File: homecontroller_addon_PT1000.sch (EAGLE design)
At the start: 44 parts, among them U1 OPA2188AIDGKR, U2 OPA2188AIDGKR, U3 REF3025AIDBZTG4, U4 ADS1015IDGST, X1 S2L3.50/10/90G

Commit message: update routing
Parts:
- added C10: 1000pF, supply2:C1206C102KDRACTU
- added R26: 0 Ohms, Vishay_By_element14_Batch_1:CRCW12060000Z0EA
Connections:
- net N$5 renamed -IN_0
- removed net +IN_1: R12.2, U1.+IN_B
- removed net +IN_2: R19.2, U2.+IN_A
- removed net +IN_3: R25.2, U2.+IN_B
- removed net N$1: R6.2, U1.+IN_A
- new net PE: C10.C1, RV1.1, RV2.1, RV3.1, RV4.1
- new net SGND: C1.C1, C4.C1, C8.C1, C9.C1, R26.2
- net AGND: now also C10.C2, R26.1, X1.2, X1.4, X1.6, X1.8; no longer C1.C1, C4.C1, C8.C1, C9.C1, RV1.1, RV2.1, RV3.1, RV4.1, X1.1, X1.3, X1.5, X1.7
- net PT1000_0: now also R6.2, U1.+IN_A, X1.1; no longer X1.2
- net PT1000_1: now also R12.2, U1.+IN_B, X1.3; no longer X1.4
- net PT1000_2: now also R19.2, U2.+IN_A, X1.5; no longer X1.6
- net PT1000_3: now also R25.2, U2.+IN_B, X1.7; no longer X1.8
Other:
- moved on the sheet: R11, R18, R24, R5

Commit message: production status
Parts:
- U4: device strasys_standard:ADS1015IDGST -> ADS1015:ADS1015IDGST
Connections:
- net +3.3V: now also X2.10; no longer X2.1
- net AGND: now also X2.1; no longer X2.10
- net AIN2: now also U4.NC_2; no longer U4.AIN2
- net AIN3: now also U4.NC; no longer U4.AIN3
- net I2C1_SCL: now also X2.3; no longer X2.8
- net I2C1_SDA: now also X2.4; no longer X2.7
- net P9_14: now also X2.7; no longer X2.4
- net P9_15: now also X2.8; no longer X2.3
- net P9_16: now also X2.9; no longer X2.2
- net UART2_RXD: now also X2.6; no longer X2.5
- net UART2_TXD: now also X2.5; no longer X2.6
- net VDD5V_F: now also X2.2; no longer X2.9
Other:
- moved on the sheet: X2

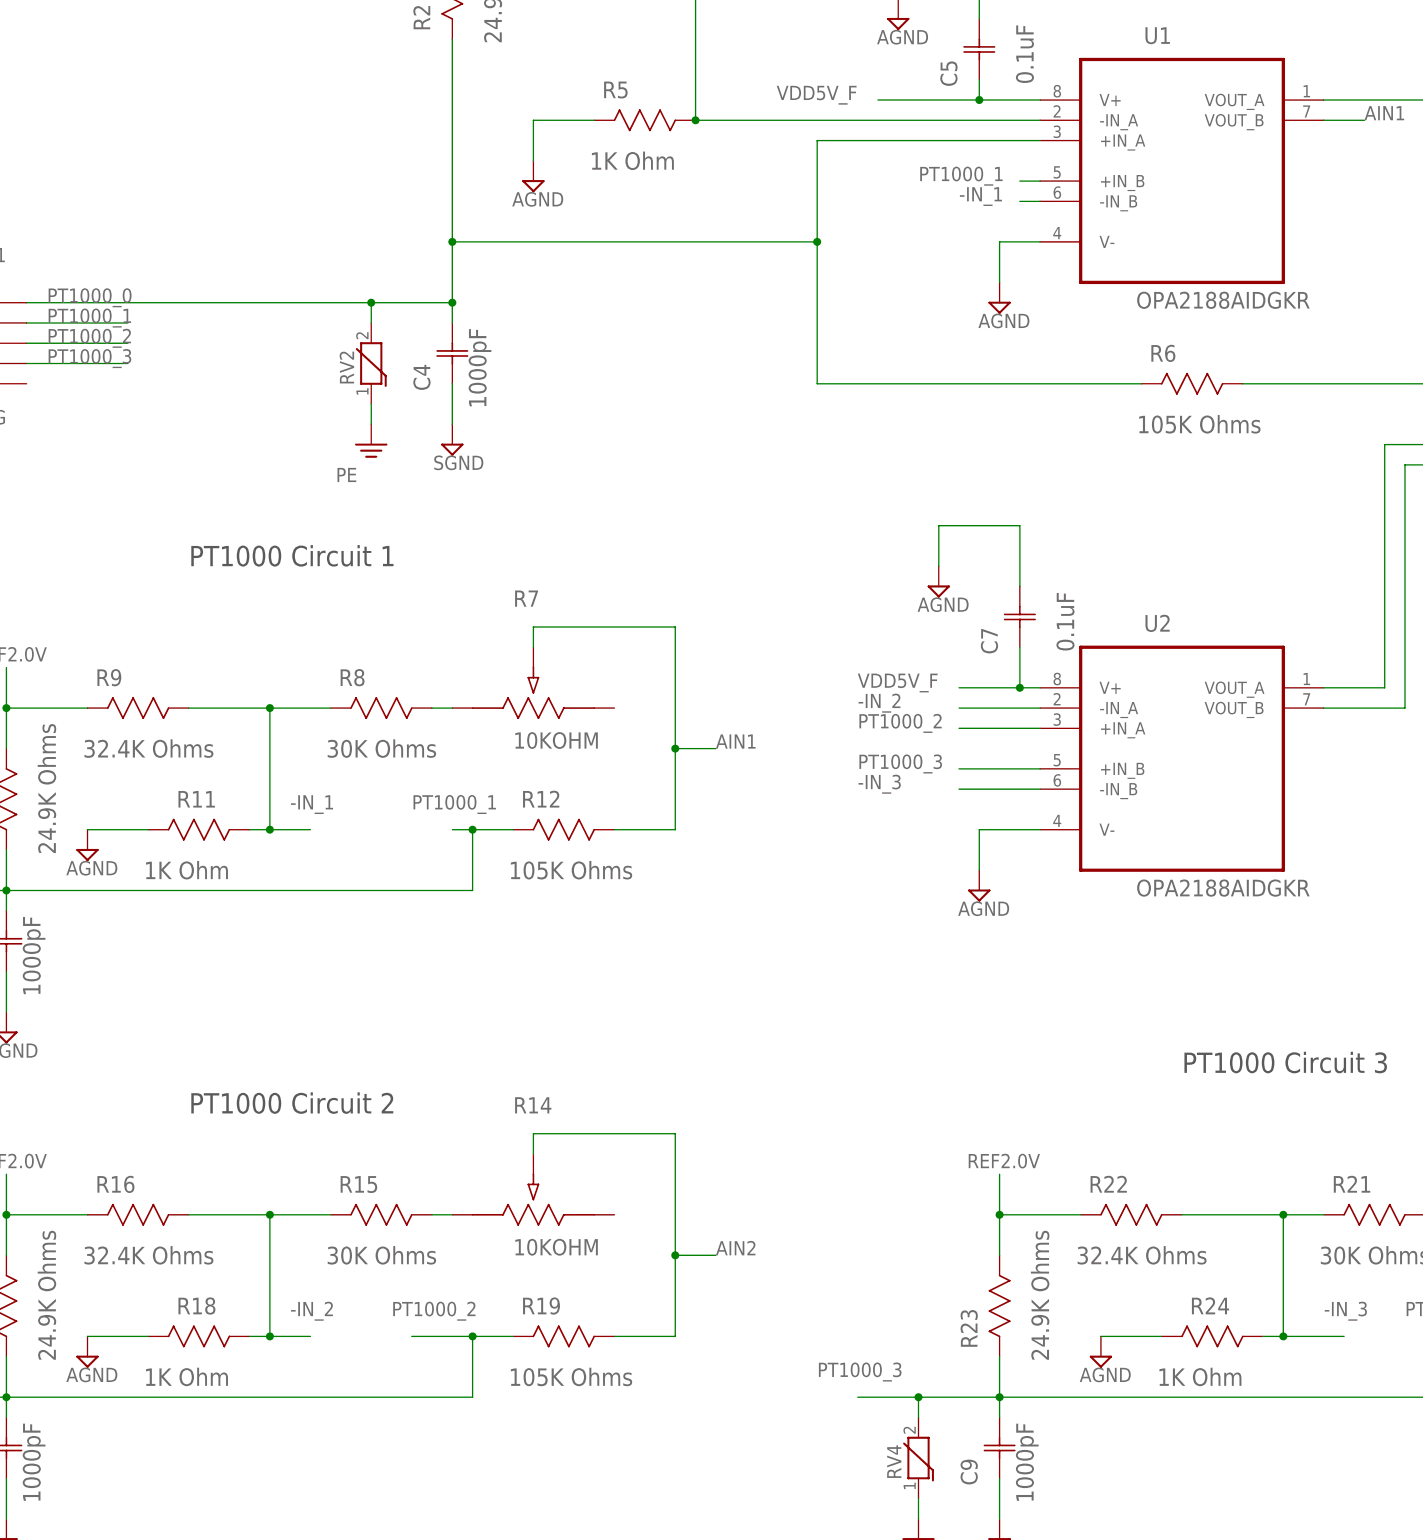
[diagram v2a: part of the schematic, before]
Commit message: components price opti
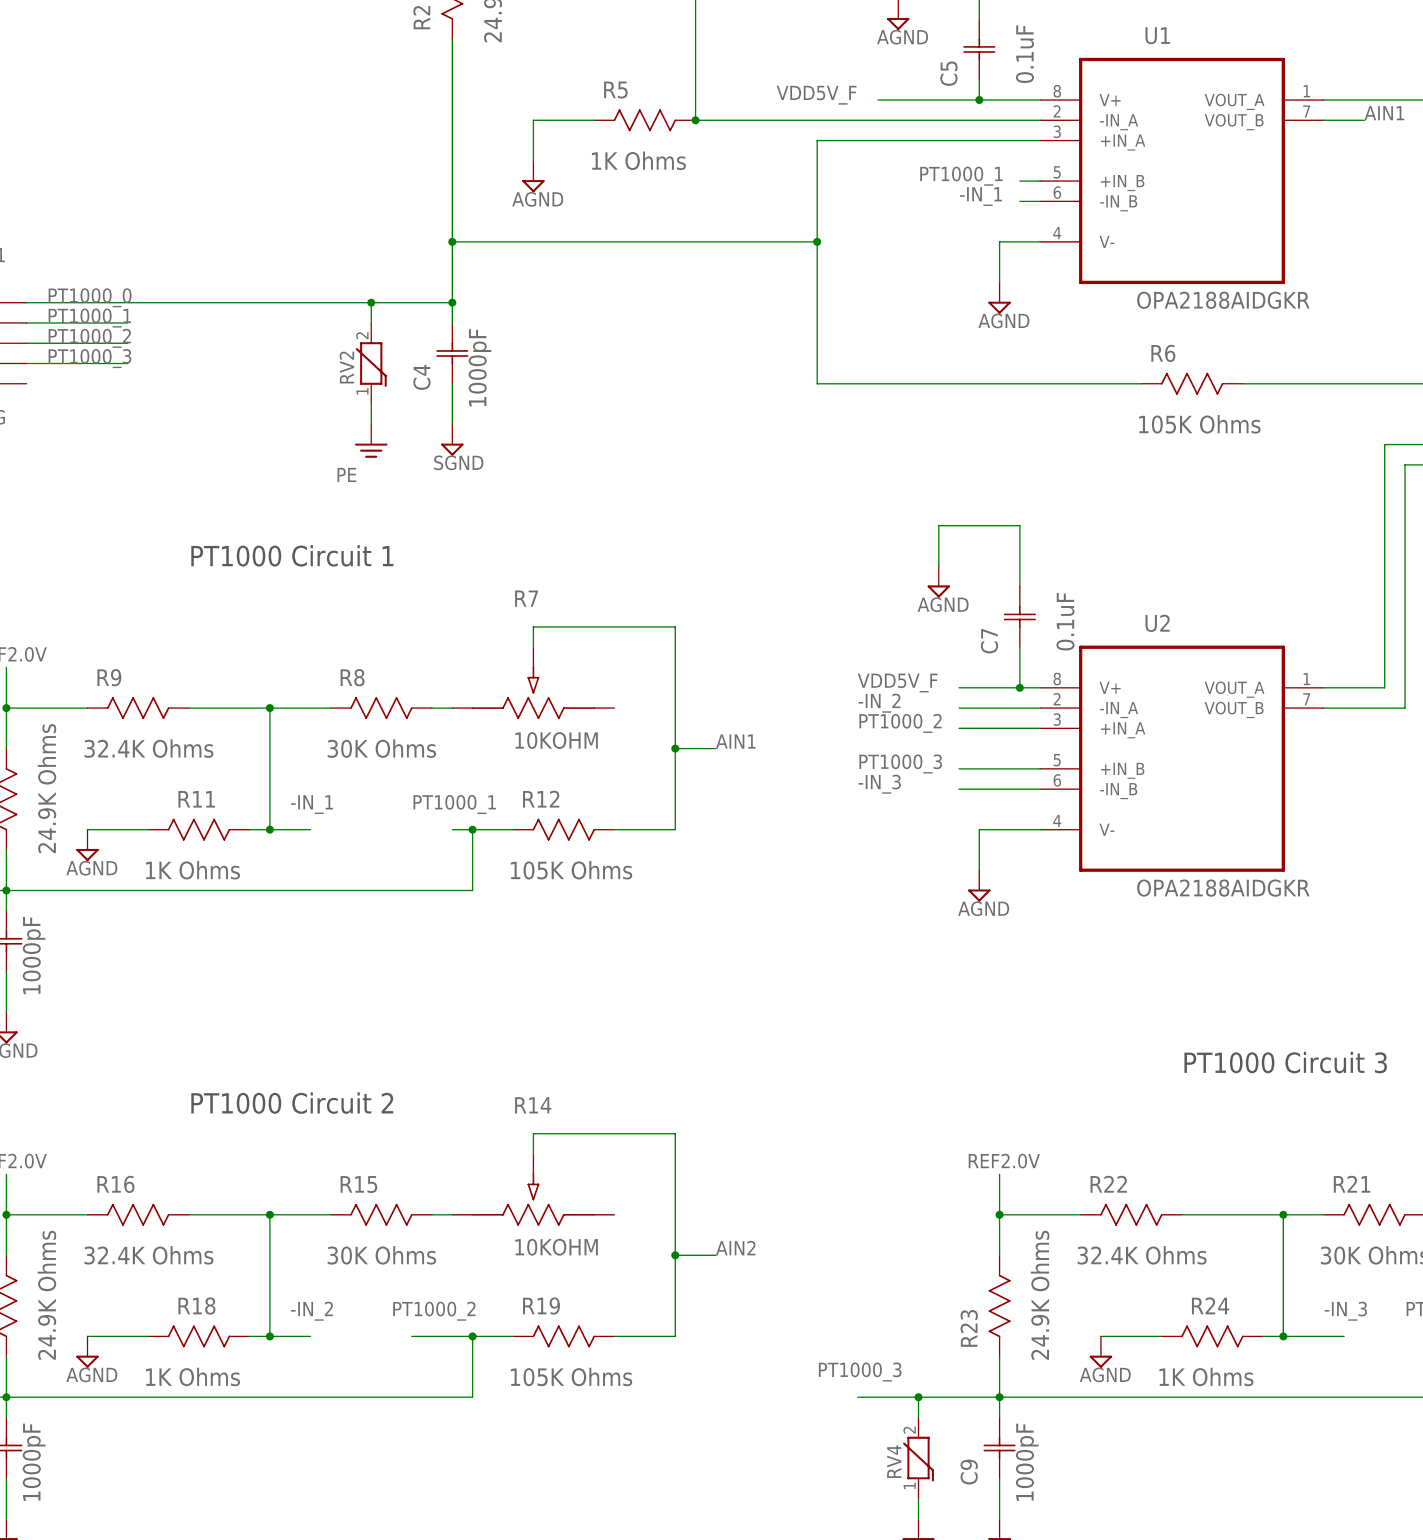
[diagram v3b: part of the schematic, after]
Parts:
- C1, C10, C4, C8, C9: MF (none) -> KEMET; OC_FARNELL (none) -> 1826304
- C2, C3, C5, C6, C7: MF (none) -> KEMET
- R1, R14, R20, R7: MF (none) -> PANASONIC ELECTRONIC COMPONENTS; OC_FARNELL (none) -> 1849801
- R10, R12, R13, R15, R17, R19, R2, R21, R23, R25, R26, R3, R6, R8: MF (none) -> VISHAY DRALORIC
- R11, R18, R24, R5: value 1K Ohm -> 1K Ohms; device Vishay_By_element14_Batch_1:CRCW08051K00FKTC -> Vishay_By_element14_Batch_1:CRCW08051K00FKEA; MF (none) -> VISHAY DRALORIC
- R16, R22, R4, R9, X1, X2: OC_FARNELL (none) -> unknown
- RV1, RV2, RV3, RV4: MF (none) -> WURTH ELEKTRONIK
- U1, U2: MF (none) -> TEXAS INSTRUMENTS; OC_FARNELL (none) -> 2057091
- U3, U4: MF (none) -> TEXAS INSTRUMENTS
